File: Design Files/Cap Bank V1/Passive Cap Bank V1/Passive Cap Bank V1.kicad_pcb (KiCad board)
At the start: 2 copper layers, 75 x 125 mm, 46 parts, among them J1 XT30-Male, Q1 BC817-40, Q2 BC817-40, Q3 BC817-40, Q4 BC817-40, Q5 BC817-40, Q6 BC817-40, SW1 SW_Push_Open

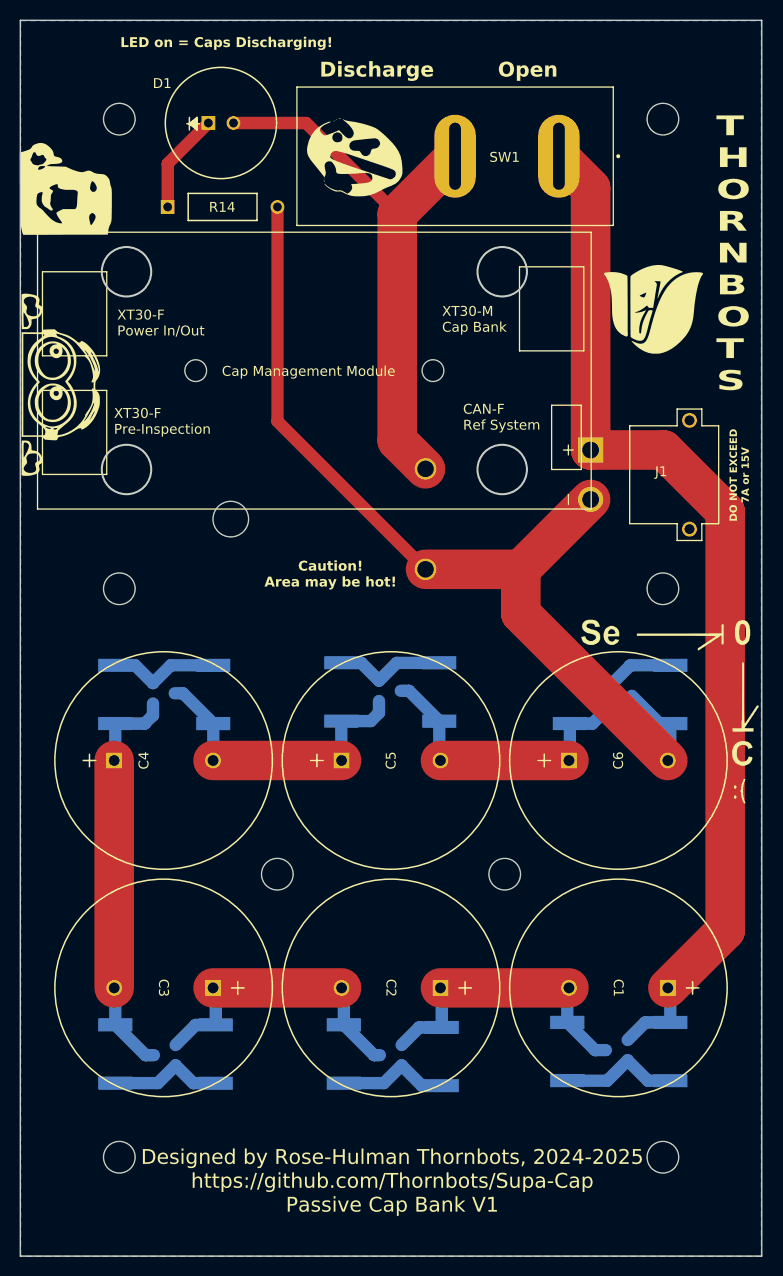
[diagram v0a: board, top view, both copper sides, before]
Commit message: Added footprint for other cap, also fixed holes not being electically isolated
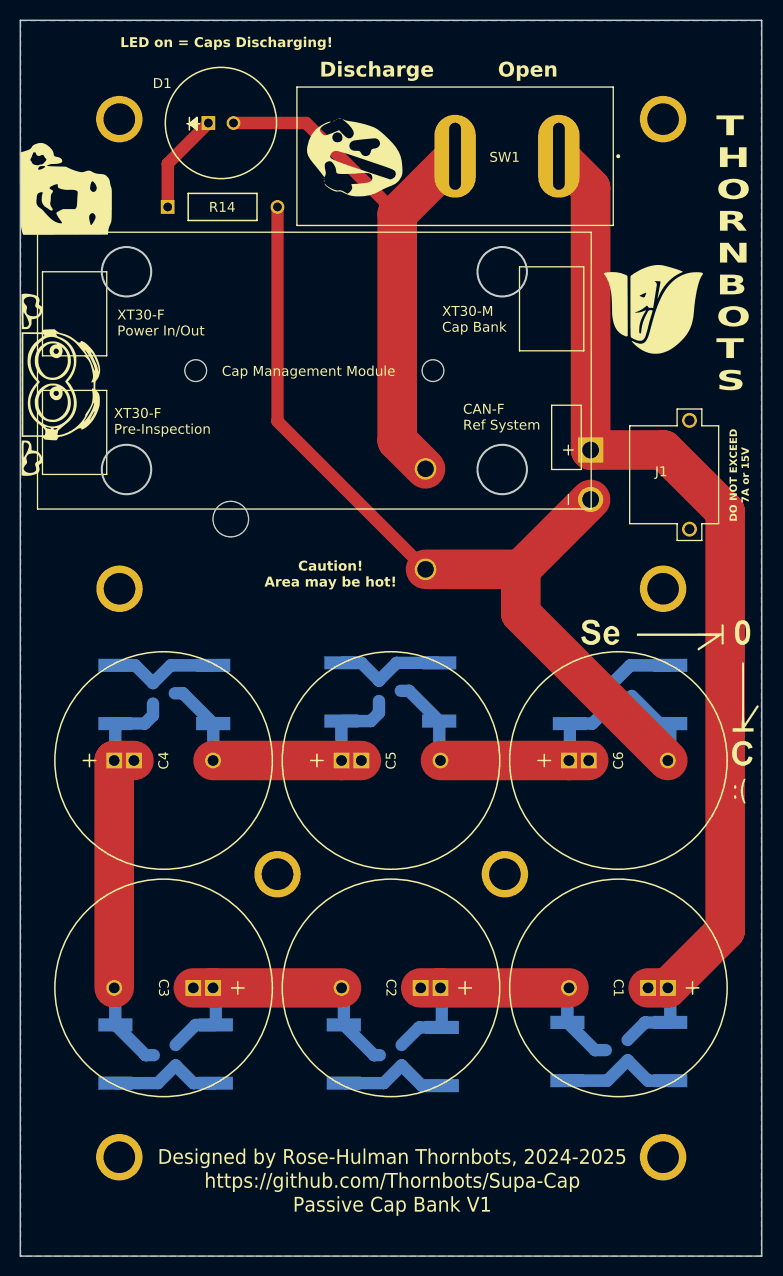
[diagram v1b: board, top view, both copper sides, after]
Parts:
- removed the G*** at (87.6, 136.4)
- added G***: LOGO, LOGO, B.Cu at (111.8, 136.6)
- added G***: LOGO, LOGO, B.Cu at (87.6, 136.1)
- C1, C2, C3, C4, C5, C6: footprint PGA460TW:100F Kyocera Cap -> PassiveBankV1:100F Kyocera Cap
- REF** (x8): footprint MountingHole:MountingHole_3.2mm_M3 -> PassiveBankV1:MountingHole_3.2mm_M3
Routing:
- net Net-(C5--): track 30.8 -> 32.8 mm
- net V_15: track 106.5 -> 108.5 mm
- net Net-(C4--): track 31.3 -> 33.3 mm
- net Net-(C3--): track 41.1 -> 43.1 mm
- net Net-(C2--): track 30.5 -> 32.5 mm
- net Net-(C1--): track 30.5 -> 32.5 mm
